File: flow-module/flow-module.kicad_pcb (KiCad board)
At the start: 2 copper layers, 60 x 47.2 mm, 22 parts, among them P1 12V, P2 tL298P, P3 tLMD..., P4 fL298P, P5 fLMD...

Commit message: PCB Design update
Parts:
- removed D1, D2, D3, D4: D, ValveTeam:do219ab
- removed D7: VSS, LEDs:LED_0805_HandSoldering
- removed H1: L298P, ValveTeam:powerso-20
- removed P2: tL298P, ValveTeam:Molex_KK-6410-06_06x2.54mm_Straight
- removed P4: fL298P, ValveTeam:TE_TERM
- removed R3: 330, Resistors_SMD:R_0805_HandSoldering
- removed REF** (x3): MountingHole_3.2mm_M3, Mounting_Holes:MountingHole_3.2mm_M3
- D5: value VCC -> LED
- D6: value VAA -> LED
- P1: value 12V -> TERM_01X02
- P3: value tLMD... -> MOLEX_01X06
- P5: value fLMD... -> TERM_01X02
- moved P5 57.6 mm to (74.9, 30.5)
- moved P1 35.6 mm to (113.0, 27.9), turned to 90 degrees
- moved P3 30.2 mm to (74.9, 52.1), turned to 90 degrees
- moved R1 23.9 mm to (95.2, 54.6), turned to 0 degrees
- moved D5 22.6 mm to (87.6, 54.6), turned to 180 degrees
- moved R2 15.3 mm to (95.2, 50.8), turned to 0 degrees
- moved D6 15.3 mm to (87.5, 50.8), turned to 180 degrees
- moved H2 10.1 mm to (104.6, 40.6)
- moved C1 9.25 mm to (82.5, 38.1)
- moved C2 8.52 mm to (110.5, 38.1), turned to 270 degrees
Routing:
- net Net-(D3-Pad2): track 69.9 -> 0.00 mm
- net Net-(D1-Pad2): track 66.5 -> 0.00 mm
- net VAA: track 77.2 -> 13.3 mm, vias 1 -> 0
- net VSS: track 61.9 -> 0.00 mm
- net Input3: track 42.8 -> 0.00 mm, vias 1 -> 0
- net Input4: track 39.0 -> 0.00 mm
- net Output2: track 51.3 -> 16.5 mm
- net VCC: track 86.8 -> 53.0 mm, vias 1 -> 0
- net PWM: track 19.8 -> 51.3 mm
- net Flag: track 15.8 -> 42.4 mm
- net Dir: track 16.8 -> 30.7 mm
- net Earth: track 57.8 -> 69.3 mm, vias 6 -> 0
- net Output1: track 29.3 -> 40.3 mm
- net Brake: track 22.2 -> 29.3 mm
- net Net-(C2-Pad1): track 6.14 -> 11.2 mm
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- removed copper zone on B.Cu, net Earth
- removed copper zone on F.Cu, net Earth
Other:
- board size 60 x 47.2 mm -> 49.5 x 35.6 mm

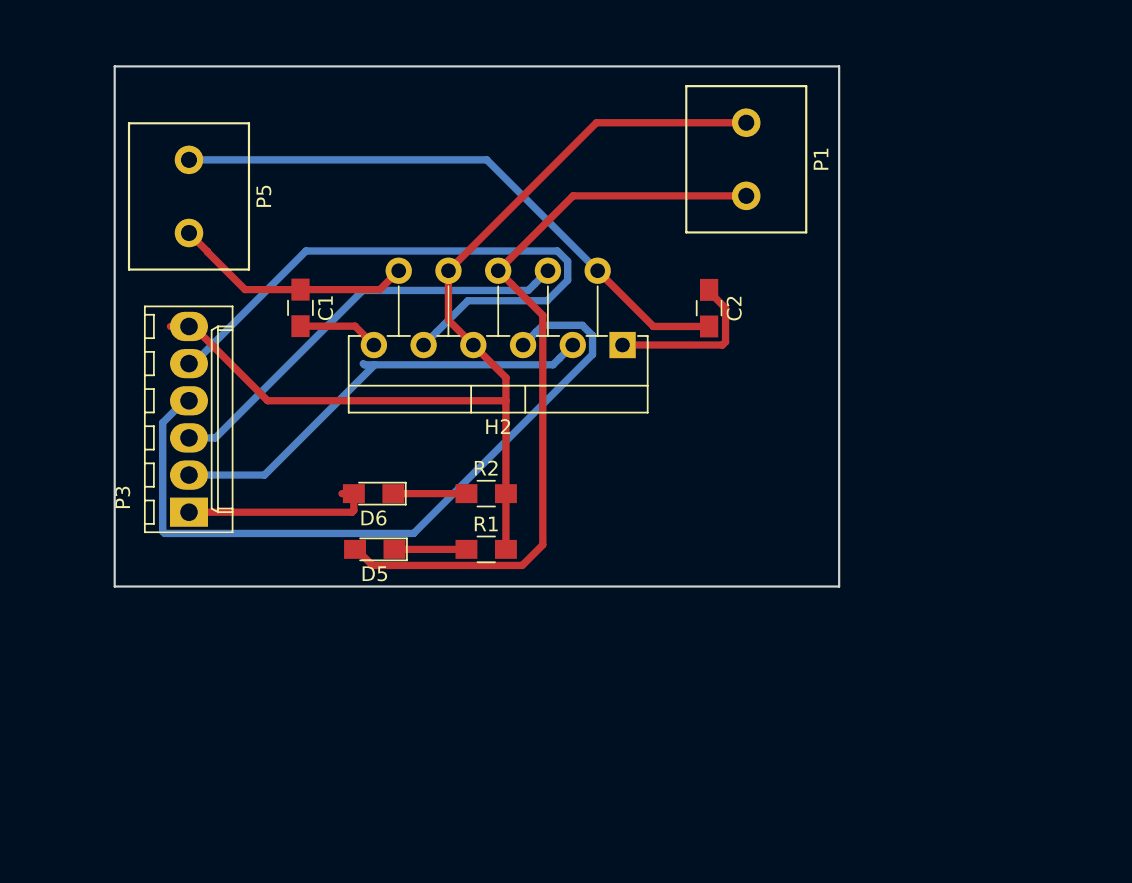
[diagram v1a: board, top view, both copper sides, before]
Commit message: Added ground planes and remove unnecessary tracks
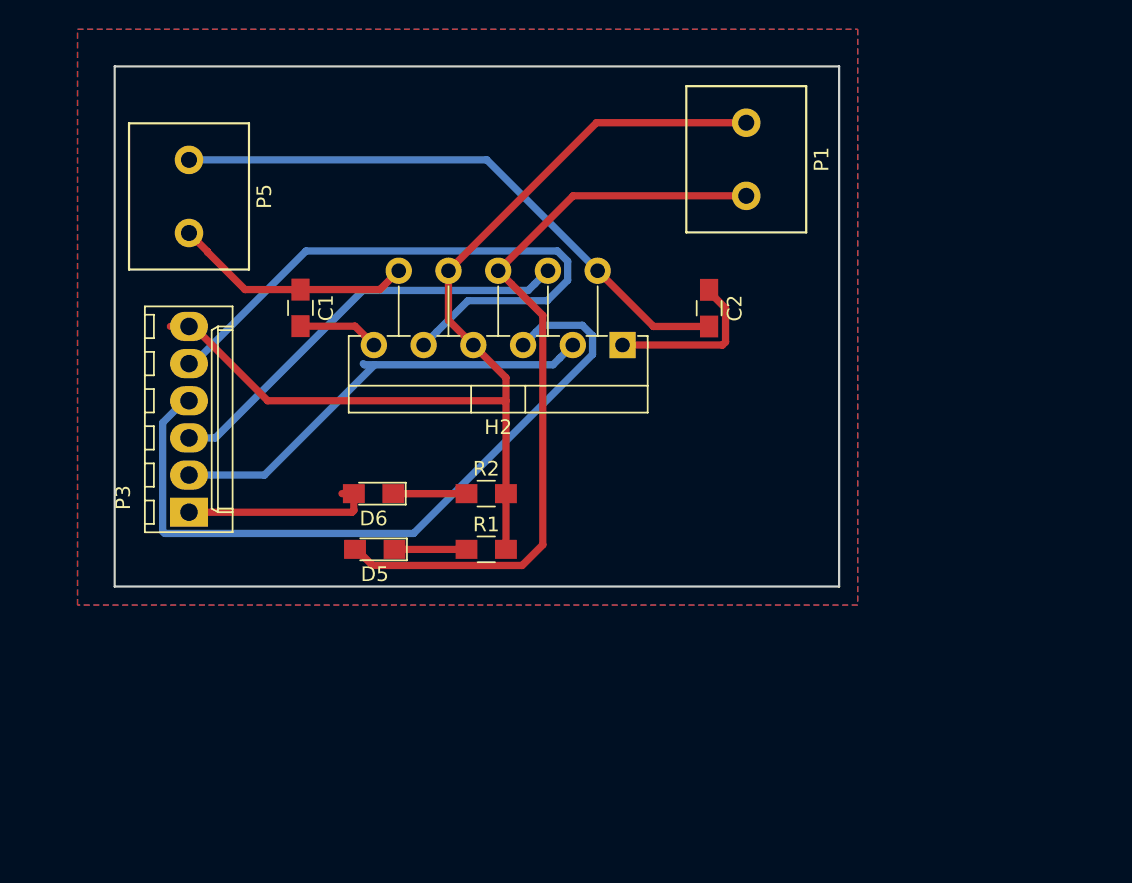
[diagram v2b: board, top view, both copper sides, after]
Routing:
- added copper zone on B.Cu, net Earth
- added copper zone on F.Cu, net Earth
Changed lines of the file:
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@@
   (general
     (links 20)
-    (no_connects 6)
-    (area 69.524999 21.924999 129.675001 69.275001)
+    (no_connects 0)
+    (area 68.725 21.514999 119.455001 57.285)
     (thickness 1.6)
     (drawings 4)
@@
   (segment (start 93.999989 37.610011) (end 91.869999 39.740001) (width 0.5) (layer B.Cu) (net 13))
   (segment (start 91.869999 39.740001) (end 90.97 40.64) (width 0.5) (layer B.Cu) (net 13))
+  (zone (net 6) (net_name Earth) (layer F.Cu) (hatch edge 0.508)
+    (connect_pads (clearance 0.508))
+    (min_thickness 0.254)
+    (fill yes (arc_segments 16) (thermal_gap 0.508) (thermal_bridge_width 0.508))
+    (polygon
+      (pts
+        (xy 67.31 19.05) (xy 120.65 19.05) (xy 120.65 58.42) (xy 67.31 58.42)
+      )
+    )
+  )
+  (zone (net 6) (net_name Earth) (layer B.Cu) (hatch edge 0.508)
+    (connect_pads (clearance 0.508))
+    (min_thickness 0.254)
+    (fill yes (arc_segments 16) (thermal_gap 0.508) (thermal_bridge_width 0.508))
+    (polygon
+      (pts
+        (xy 67.31 19.05) (xy 120.65 19.05) (xy 120.65 58.42) (xy 67.31 58.42)
+      )
+    )
+  )
 )
